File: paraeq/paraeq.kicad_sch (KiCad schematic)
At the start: 33 parts, among them J1 Input, J2 Series, J3 Output, SW1 Bypass, U1 Opamp_Dual, U2 Opamp_Quad

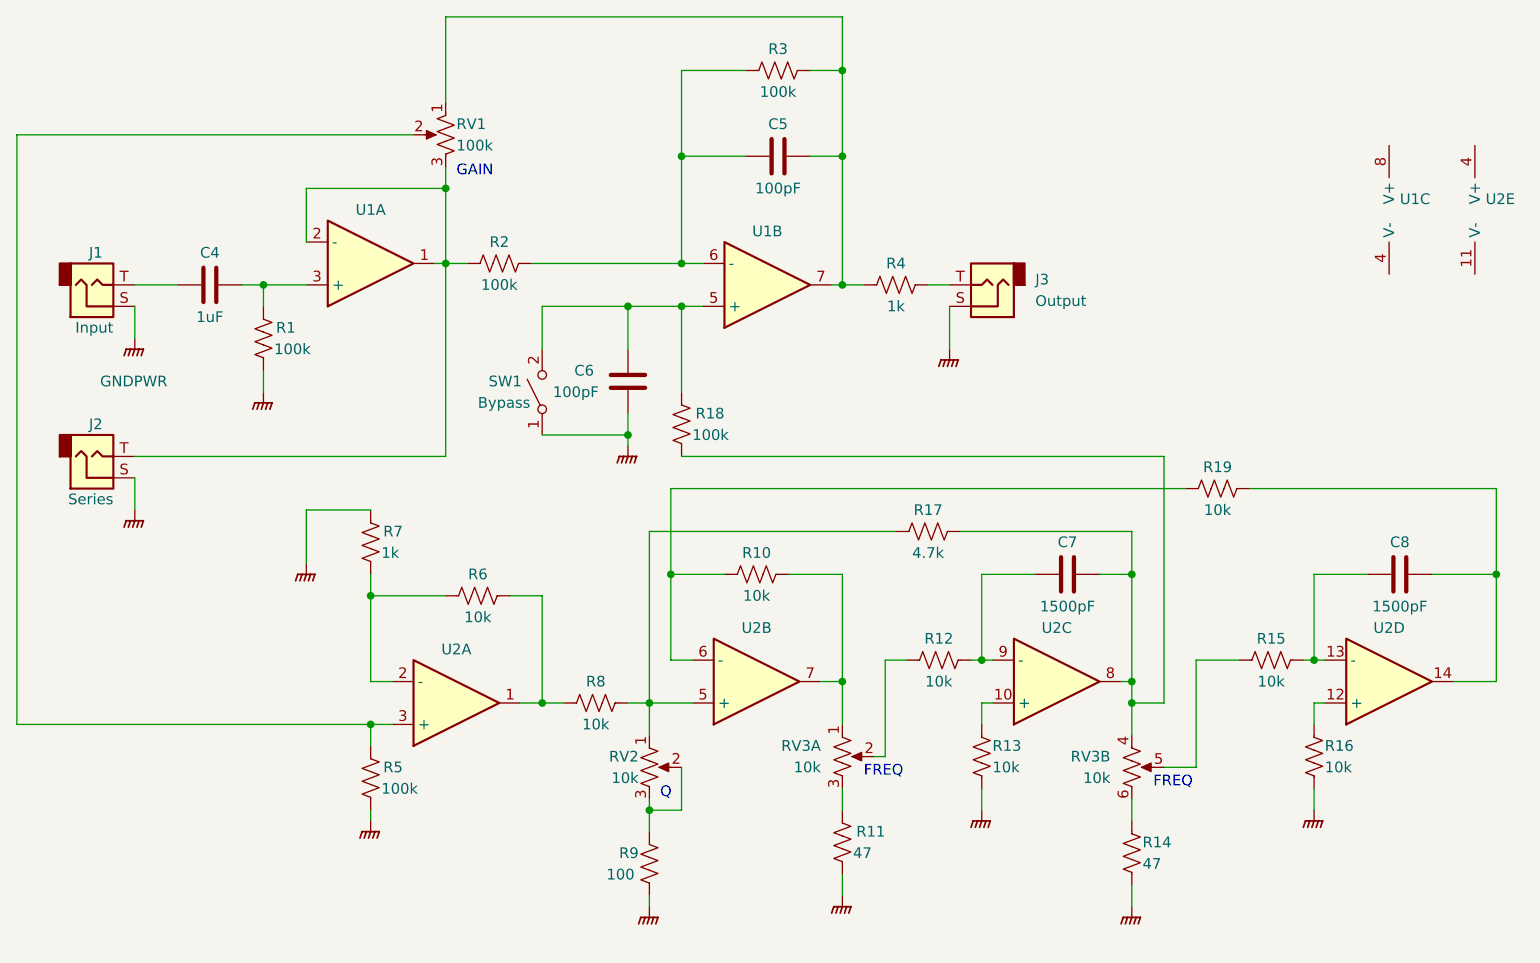
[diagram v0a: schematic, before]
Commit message: Finished parametric equalizer.
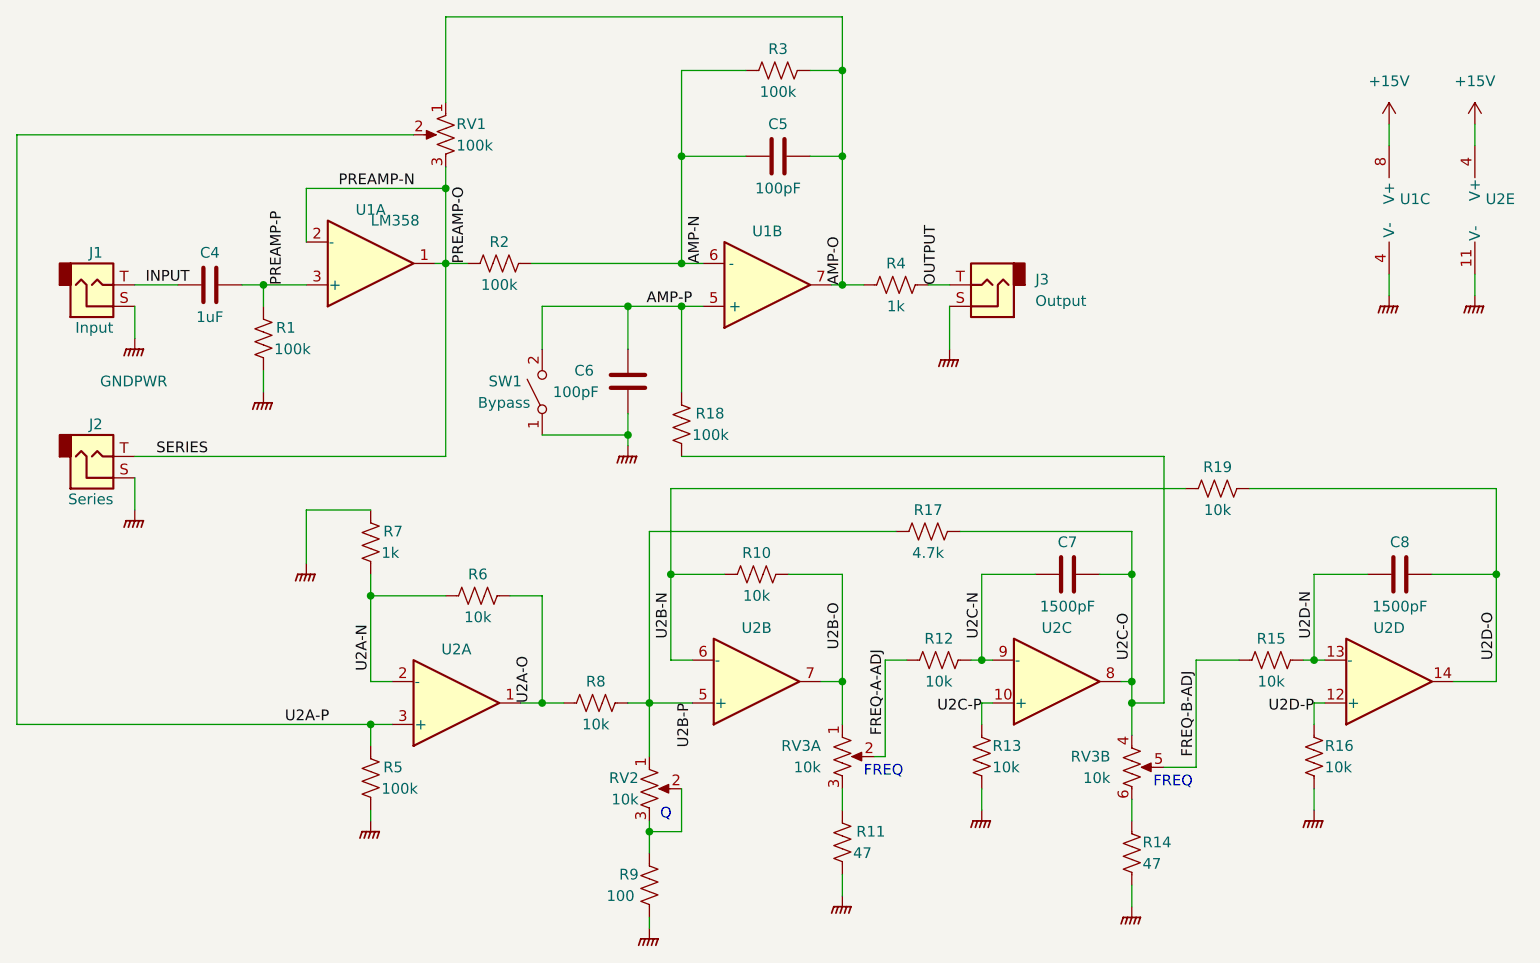
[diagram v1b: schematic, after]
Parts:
- C4, C5, C6, C7, C8: footprint (none) -> Capacitor_SMD:C_0805_2012Metric_Pad1.18x1.45mm_HandSolder
- J1, J2, J3: footprint (none) -> Connector_Audio:Jack_3.5mm_CUI_SJ1-3523N_Horizontal
- R1, R10, R11, R12, R13, R14, R15, R16, R17, R18, R19, R2, R3, R4, R5, R6, R7, R8, R9: footprint (none) -> Resistor_SMD:R_0805_2012Metric_Pad1.20x1.40mm_HandSolder
- RV1, RV2: footprint (none) -> Connector_Wire:SolderWire-0.1sqmm_1x03_P3.6mm_D0.4mm_OD1mm
- RV3: footprint (none) -> audio-project:SolderWire-0.1sqmm_2x03_P3.6mm_D0.4mm_OD1mm
- SW1: footprint (none) -> Connector_Wire:SolderWire-0.1sqmm_1x02_P3.6mm_D0.4mm_OD1mm
- U1: value Opamp_Dual -> LM358; footprint (none) -> Package_SO:SOIC-8_3.9x4.9mm_P1.27mm
- U1: value Opamp_Dual -> LM358; footprint (none) -> Package_SO:SOIC-8_3.9x4.9mm_P1.27mm; symbol Device:Opamp_Dual -> Amplifier_Operational:LM358
- U2: value Opamp_Quad -> LM324; footprint (none) -> Package_SO:SOIC-14_3.9x8.7mm_P1.27mm; symbol Device:Opamp_Quad -> Amplifier_Operational:LM324
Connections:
- net GNDPWR: now also U1.4 (V-), U2.11 (V-)
- net AMP-P: now reaches C6.1, R18.1, SW1.2 (B), U1.5 (+)
- net AMP-N: now reaches C5.1, R2.2, R3.1, U1.6 (-)
- net AMP-O: now reaches C5.2, R3.2, R4.1, RV1.1, U1.7
- net U2C-N: now reaches C7.1, R12.2, U2.9 (-)
- net U2C-O: now reaches C7.2, R17.2, R18.2, RV3.4, U2.8
- net +15V: now reaches U2.4 (V+)
- net +15V: now also U1.8 (V+)
- net U2D-P: now reaches R16.1, U2.12 (+)
- net OUTPUT: now reaches J3.T, R4.2
- net U2C-P: now reaches R13.1, U2.10 (+)
- net INPUT: now reaches C4.1, J1.T
- net FREQ-A-ADJ: now reaches R12.1, RV3.2
- net PREAMP-P: now reaches C4.2, R1.1, U1.3 (+)
- net PREAMP-N: now reaches J2.T, R2.1, RV1.3, U1.1, U1.2 (-)
- net U2B-P: now reaches R17.1, R8.2, RV2.1, U2.5 (+)
- net U2A-P: now reaches R5.1, RV1.2, U2.3 (+)
- net FREQ-B-ADJ: now reaches R15.1, RV3.5
- net U2A-N: now reaches R6.1, R7.2, U2.2 (-)
- net U2D-N: now reaches C8.1, R15.2, U2.13 (-)
- net U2D-O: now reaches C8.2, R19.2, U2.14
- net U2B-N: now reaches R10.1, R19.1, U2.6 (-)
- net U2B-O: now reaches R10.2, RV3.1, U2.7
- net U2A-O: now reaches R6.2, R8.1, U2.1
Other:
- note removed: "GAIN"
- moved on the sheet: R9, RV2
